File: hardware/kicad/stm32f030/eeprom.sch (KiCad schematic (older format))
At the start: 1 part, among them IC1 AT24CS02-SSHM

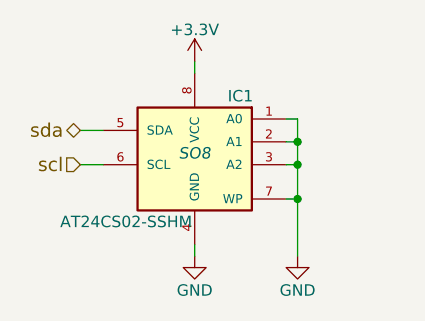
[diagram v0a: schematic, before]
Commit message: hardware/kicad/stm32f030: adding eeprom step2
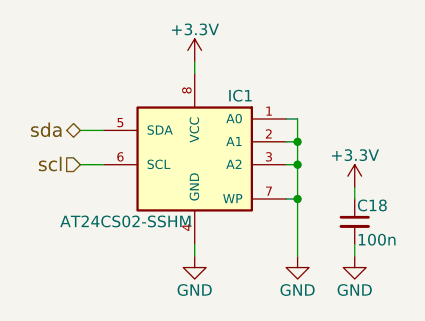
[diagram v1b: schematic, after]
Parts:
- added C18: 100n, Capacitors_SMD:C_0805_HandSoldering, symbol C_Small
- IC1: footprint SO8 -> Housings_SOIC:SOIC-8_3.9x4.9mm_Pitch1.27mm
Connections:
- net +3V3: now also C18.1
- net GND: now also C18.2
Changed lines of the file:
@@
 F 0 "IC1" H 5400 3500 50  0000 C CNN
 F 1 "AT24CS02-SSHM" H 5900 2950 50  0000 C CNN
-F 2 "SO8" H 5600 3250 50  0000 C CIN
+F 2 "Housings_SOIC:SOIC-8_3.9x4.9mm_Pitch1.27mm" H 5600 3250 50  0001 C CIN
 F 3 "" H 5600 3250 50  0000 C CNN
 	1    5600 3250
@@
 $EndComp
 $Comp
-L GND #PWR56
+L GND #PWR57
 U 1 1 589C2085
 P 5600 3700
-F 0 "#PWR56" H 5600 3450 50  0001 C CNN
+F 0 "#PWR57" H 5600 3450 50  0001 C CNN
 F 1 "GND" H 5600 3550 50  0000 C CNN
 F 2 "" H 5600 3700 50  0000 C CNN
@@
 	6050 3300 6000 3300
 $Comp
-L GND #PWR57
+L GND #PWR58
 U 1 1 589C239F
 P 6050 3700
-F 0 "#PWR57" H 6050 3450 50  0001 C CNN
+F 0 "#PWR58" H 6050 3450 50  0001 C CNN
 F 1 "GND" H 6050 3550 50  0000 C CNN
 F 2 "" H 6050 3700 50  0000 C CNN
@@
 Wire Wire Line
 	5600 2900 5600 2850
+$Comp
+L C_Small C18
+U 1 1 589CB0CF
+P 6300 3550
+F 0 "C18" H 6310 3620 50  0000 L CNN
+F 1 "100n" H 6310 3470 50  0000 L CNN
+F 2 "Capacitors_SMD:C_0805_HandSoldering" H 6300 3550 50  0001 C CNN
+F 3 "" H 6300 3550 50  0000 C CNN
+	1    6300 3550
+	1    0    0    -1
+$EndComp
+$Comp
+L +3.3V #PWR56
+U 1 1 589CB128
+P 6300 3400
+F 0 "#PWR56" H 6300 3250 50  0001 C CNN
+F 1 "+3.3V" H 6300 3540 50  0000 C CNN
+F 2 "" H 6300 3400 50  0000 C CNN
+F 3 "" H 6300 3400 50  0000 C CNN
+	1    6300 3400
+	1    0    0    -1
+$EndComp
+$Comp
+L GND #PWR59
+U 1 1 589CB139
+P 6300 3700
+F 0 "#PWR59" H 6300 3450 50  0001 C CNN
+F 1 "GND" H 6300 3550 50  0000 C CNN
+F 2 "" H 6300 3700 50  0000 C CNN
+F 3 "" H 6300 3700 50  0000 C CNN
+	1    6300 3700
+	1    0    0    -1
+$EndComp
+Wire Wire Line
+	6300 3700 6300 3650
+Wire Wire Line
+	6300 3450 6300 3400
 $EndSCHEMATC

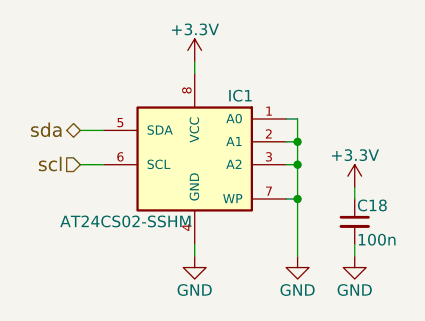
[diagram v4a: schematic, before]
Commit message: hardware/kicad/stm32f030: everything is connected, DRC OK
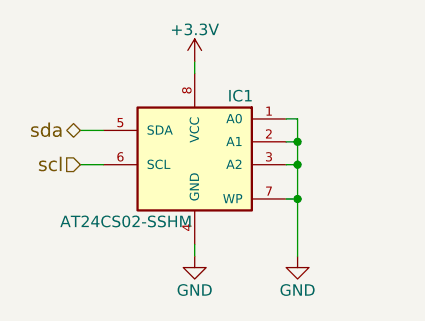
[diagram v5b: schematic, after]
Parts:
- removed C18: 100n, Capacitors_SMD:C_0805_HandSoldering, symbol C_Small
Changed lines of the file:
@@
 LIBS:transformer
 LIBS:stm32
+LIBS:switches
 LIBS:stm32f030-cache
 EELAYER 25 0
@@
 $Descr A4 11693 8268
 encoding utf-8
-Sheet 6 5
+Sheet 5 5
 Title ""
 Date ""
@@
 Wire Wire Line
 	5600 2900 5600 2850
-$Comp
-L C_Small C18
-U 1 1 589CB0CF
-P 6300 3550
-F 0 "C18" H 6310 3620 50  0000 L CNN
-F 1 "100n" H 6310 3470 50  0000 L CNN
-F 2 "Capacitors_SMD:C_0805_HandSoldering" H 6300 3550 50  0001 C CNN
-F 3 "" H 6300 3550 50  0000 C CNN
-	1    6300 3550
-	1    0    0    -1
-$EndComp
-$Comp
-L +3.3V #PWR048
-U 1 1 589CB128
-P 6300 3400
-F 0 "#PWR048" H 6300 3250 50  0001 C CNN
-F 1 "+3.3V" H 6300 3540 50  0000 C CNN
-F 2 "" H 6300 3400 50  0000 C CNN
-F 3 "" H 6300 3400 50  0000 C CNN
-	1    6300 3400
-	1    0    0    -1
-$EndComp
-$Comp
-L GND #PWR049
-U 1 1 589CB139
-P 6300 3700
-F 0 "#PWR049" H 6300 3450 50  0001 C CNN
-F 1 "GND" H 6300 3550 50  0000 C CNN
-F 2 "" H 6300 3700 50  0000 C CNN
-F 3 "" H 6300 3700 50  0000 C CNN
-	1    6300 3700
-	1    0    0    -1
-$EndComp
-Wire Wire Line
-	6300 3700 6300 3650
-Wire Wire Line
-	6300 3450 6300 3400
 $EndSCHEMATC
